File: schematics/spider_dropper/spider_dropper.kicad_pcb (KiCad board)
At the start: 2 copper layers, 80 x 20 mm, 10 parts, among them J1 12V DC, J2 JST_XH_3, J3 JST_XH_2, Q1 IRLZ34N, SW1 ZX40E20C01

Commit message: I think I'm ready to order Rev. D PCBs.
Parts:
- J2: renamed from J1; value 12V DC -> PJ-044AH
- renumbered J2 to J1
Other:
- board text added: "GND"
- board text added: "VIN"
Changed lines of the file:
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@@
 	(net 1 "+12V")
 	(net 2 "GND")
-	(net 3 "unconnected-(J1-Pad3)")
-	(net 4 "unconnected-(SW1-C-Pad2)")
-	(net 5 "/MOTOR+")
-	(net 6 "/MOTOR-")
-	(net 7 "/MOTION")
+	(net 3 "unconnected-(SW1-C-Pad2)")
+	(net 4 "/MOTOR+")
+	(net 5 "/MOTOR-")
+	(net 6 "/MOTION")
+	(net 7 "unconnected-(J2-Pad3)")
 	(footprint "Diode_THT:D_A-405_P7.62mm_Horizontal"
 		(layer "F.Cu")
@@
 			(remove_unused_layers no)
 			(roundrect_rratio 0.138889)
-			(net 5 "/MOTOR+")
+			(net 4 "/MOTOR+")
 			(pinfunction "K")
 			(pintype "passive")
@@
 			(layers "*.Cu" "*.Mask")
 			(remove_unused_layers no)
-			(net 6 "/MOTOR-")
+			(net 5 "/MOTOR-")
 			(pinfunction "A")
 			(pintype "passive")
@@
 			(layers "*.Cu" "*.Mask")
 			(remove_unused_layers no)
-			(net 7 "/MOTION")
+			(net 6 "/MOTION")
 			(pintype "passive")
 		)
@@
 		(at 116.5 104.8)
 		(descr "Barrel Jack, 2.0mm ID, 5.5mm OD, Vertical, THT, 5 Amp")
-		(property "Reference" "J1"
+		(property "Reference" "J2"
 			(at 4.2 8.1 0)
 			(unlocked yes)
@@
 			)
 		)
-		(property "Value" "12V DC"
+		(property "Value" "PJ-044AH"
 			(at 0 7.57 0)
 			(unlocked yes)
@@
 			(remove_unused_layers no)
 			(roundrect_rratio 0.15)
-			(net 3 "unconnected-(J1-Pad3)")
+			(net 7 "unconnected-(J2-Pad3)")
 			(pintype "passive+no_connect")
 			(thermal_bridge_angle 45)
@@
 			(remove_unused_layers no)
 			(roundrect_rratio 0.147059)
-			(net 5 "/MOTOR+")
+			(net 4 "/MOTOR+")
 			(pinfunction "Pin_1")
 			(pintype "passive")
@@
 			(layers "*.Cu" "*.Mask")
 			(remove_unused_layers no)
-			(net 6 "/MOTOR-")
+			(net 5 "/MOTOR-")
 			(pinfunction "Pin_2")
 			(pintype "passive")
@@
 			(layers "*.Cu" "*.Mask")
 			(remove_unused_layers no)
-			(net 7 "/MOTION")
+			(net 6 "/MOTION")
 			(pinfunction "G")
 			(pintype "input")
@@
 			(layers "*.Cu" "*.Mask")
 			(remove_unused_layers no)
-			(net 6 "/MOTOR-")
+			(net 5 "/MOTOR-")
 			(pinfunction "D")
 			(pintype "passive")
@@
 			(layers "*.Cu" "*.Mask")
 			(remove_unused_layers no)
-			(net 5 "/MOTOR+")
+			(net 4 "/MOTOR+")
 			(pintype "passive")
 		)
@@
 		(descr "JST XH series connector, B3B-XH-AM, with boss (http://www.jst-mfg.com/product/pdf/eng/eXH.pdf), generated with kicad-footprint-generator")
 		(tags "connector JST XH vertical boss")
-		(property "Reference" "J2"
+		(property "Reference" "J1"
 			(at 6.8 -3.375 0)
 			(layer "F.SilkS")
@@
 			(remove_unused_layers no)
 			(roundrect_rratio 0.147059)
-			(net 5 "/MOTOR+")
+			(net 4 "/MOTOR+")
 			(pinfunction "Pin_1")
 			(pintype "passive")
@@
 			(layers "*.Cu" "*.Mask")
 			(remove_unused_layers no)
-			(net 7 "/MOTION")
+			(net 6 "/MOTION")
 			(pinfunction "Pin_2")
 			(pintype "passive")
@@
 		(tags "mountinghole M3")
 		(property "Reference" "H1"
-			(at -4.3 -1.4 180)
+			(at 6.3 -1.4 180)
 			(layer "B.SilkS")
 			(effects
@@
 			(layers "*.Cu" "*.Mask")
 			(remove_unused_layers no)
-			(net 4 "unconnected-(SW1-C-Pad2)")
+			(net 3 "unconnected-(SW1-C-Pad2)")
 			(pinfunction "C")
 			(pintype "passive+no_connect")
@@
 			(layers "*.Cu" "*.Mask")
 			(remove_unused_layers no)
-			(net 6 "/MOTOR-")
+			(net 5 "/MOTOR-")
 			(pinfunction "A")
 			(pintype "passive")
@@
 	)
 	(gr_line
-		(start 172.9 113.3)
-		(end 171.4 110.7)
+		(start 175 113.3)
+		(end 175 117.1)
 		(stroke
 			(width 0.1)
-			(type default)
+			(type dot)
 		)
 		(layer "F.SilkS")
 	)
-	(gr_poly
-		(pts
-			(xy 171.4 110.7) (xy 168.4 110.7) (xy 166.8 113.3) (xy 168.4 115.9) (xy 171.4 115.9) (xy 172.9 113.3)
+	(gr_arc
+		(start 164.8 113.3)
+		(mid 169.9 108.2)
+		(end 175 113.3)
+		(stroke
+			(width 0.1)
+			(type dot)
 		)
+		(layer "F.SilkS")
+	)
+	(gr_line
+		(start 164.8 113.3)
+		(end 164.8 117.1)
 		(stroke
 			(width 0.1)
-			(type solid)
+			(type dot)
 		)
-		(fill no)
 		(layer "F.SilkS")
 	)
 	(gr_rect
-		(start 164.35 100.8)
-		(end 177.45 106.9)
+		(start 163.35 100.25)
+		(end 176.45 106.35)
 		(stroke
 			(width 0.1)
@@
 	)
 	(gr_rect
-		(start 164.35 100.8)
-		(end 177.45 106.9)
+		(start 163.35 100.25)
+		(end 176.45 106.35)
 		(stroke
 			(width 0.1)
@@
 		)
 	)
+	(gr_text "VIN"
+		(at 116.5 103.3 0)
+		(layer "F.SilkS")
+		(effects
+			(font
+				(size 1 1)
+				(thickness 0.15)
+			)
+			(justify bottom)
+		)
+	)
+	(gr_text "GND"
+		(at 116.5 109.6 0)
+		(layer "F.SilkS")
+		(effects
+			(font
+				(size 1 1)
+				(thickness 0.15)
+			)
+			(justify bottom)
+		)
+	)
 	(gr_text "Rev. D - 2025"
-		(at 171 108.5 0)
+		(at 169.9 107.9 0)
 		(layer "F.SilkS")
 		(effects
@@
 	)
 	(gr_text "Slightly Smarter\nSpider Dropper\nAdrian McCarthy"
-		(at 170.95 103.9 0)
+		(at 169.9 103.3 0)
 		(layer "F.SilkS")
 		(effects
@@
 	)
 	(gr_text "M3"
-		(at 166.7 113.3 0)
+		(at 177.3 113.3 0)
 		(layer "B.SilkS")
 		(effects
@@
 	)
 	(gr_text "Slightly Smarter\nSpider Dropper\nAdrian McCarthy"
-		(at 170.95 103.9 0)
+		(at 169.9 103.3 0)
 		(layer "B.SilkS")
 		(effects
@@
 	)
 	(gr_text "Rev. D - 2025"
-		(at 171 108.5 0)
+		(at 169.9 107.9 0)
 		(layer "B.SilkS")
 		(effects
@@
 		(width 0.2)
 		(layer "F.Cu")
-		(net 5)
+		(net 4)
 	)
 	(segment
@@
 		(width 0.2)
 		(layer "F.Cu")
-		(net 5)
+		(net 4)
 	)
 	(segment
@@
 		(width 0.2)
 		(layer "F.Cu")
-		(net 5)
+		(net 4)
 	)
 	(segment
@@
 		(width 0.2)
 		(layer "F.Cu")
-		(net 5)
+		(net 4)
 	)
 	(segment
@@
 		(width 0.2)
 		(layer "F.Cu")
-		(net 5)
+		(net 4)
 	)
 	(segment
@@
 		(width 0.2)
 		(layer "F.Cu")
-		(net 5)
+		(net 4)
 	)
 	(segment
@@
 		(width 0.2)
 		(layer "F.Cu")
-		(net 5)
+		(net 4)
 	)
 	(segment
@@
 		(width 0.2)
 		(layer "F.Cu")
-		(net 6)
+		(net 5)
 	)
 	(segment
@@
 		(width 0.2)
 		(layer "F.Cu")
-		(net 6)
+		(net 5)
 	)
 	(segment
@@
 		(width 0.2)
 		(layer "F.Cu")
-		(net 6)
+		(net 5)
 	)
 	(segment
@@
 		(width 0.2)
 		(layer "F.Cu")
-		(net 6)
+		(net 5)
 	)
 	(segment
@@
 		(width 0.2)
 		(layer "F.Cu")
-		(net 6)
+		(net 5)
 	)
 	(segment
@@
 		(width 0.2)
 		(layer "F.Cu")
-		(net 6)
+		(net 5)
 	)
 	(segment
@@
 		(width 0.2)
 		(layer "F.Cu")
-		(net 6)
+		(net 5)
 	)
 	(segment
@@
 		(width 0.2)
 		(layer "F.Cu")
-		(net 6)
+		(net 5)
 	)
 	(segment
@@
 		(width 0.2)
 		(layer "F.Cu")
-		(net 6)
+		(net 5)
 	)
 	(segment
@@
 		(width 0.2)
 		(layer "F.Cu")
-		(net 7)
+		(net 6)
 	)
 	(segment
@@
 		(width 0.2)
 		(layer "F.Cu")
-		(net 7)
+		(net 6)
 	)
 	(segment
@@
 		(width 0.2)
 		(layer "F.Cu")
-		(net 7)
+		(net 6)
 	)
 	(segment
@@
 		(width 0.2)
 		(layer "F.Cu")
-		(net 7)
+		(net 6)
 	)
 	(zone
@@
 		)
 	)
+	(group ""
+		(members "2a1c117f-9e90-49bd-96d1-d0fd1d1256d9" "8e58b6e7-301e-48f4-91da-1958e2963ec6"
+			"e5bebbb6-7bee-4a3c-8b40-823a10df51a7"
+		)
+	)

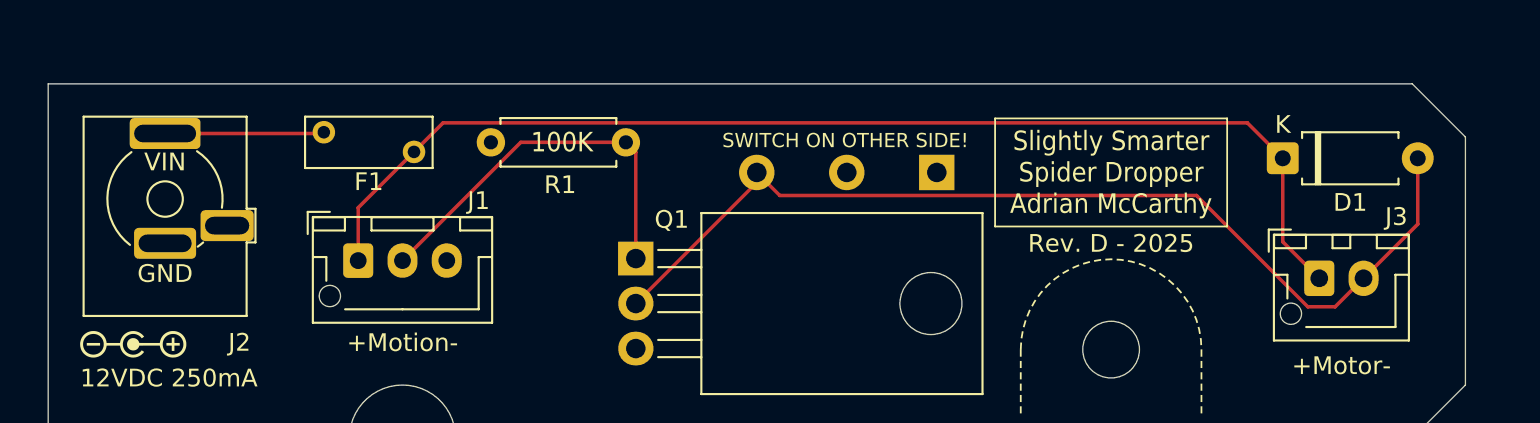
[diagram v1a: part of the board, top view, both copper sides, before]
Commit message: Updated PCB layout to Rev E.
Rev D was usable, but I discovered:

* The footprint for the vertical power jack was wrong.  I corrected it
in my footprint library and updated the PCB layout accordingly.

* The diode was a bit close to the cut corner.  I nudged it in to make
it easier to solder in place.
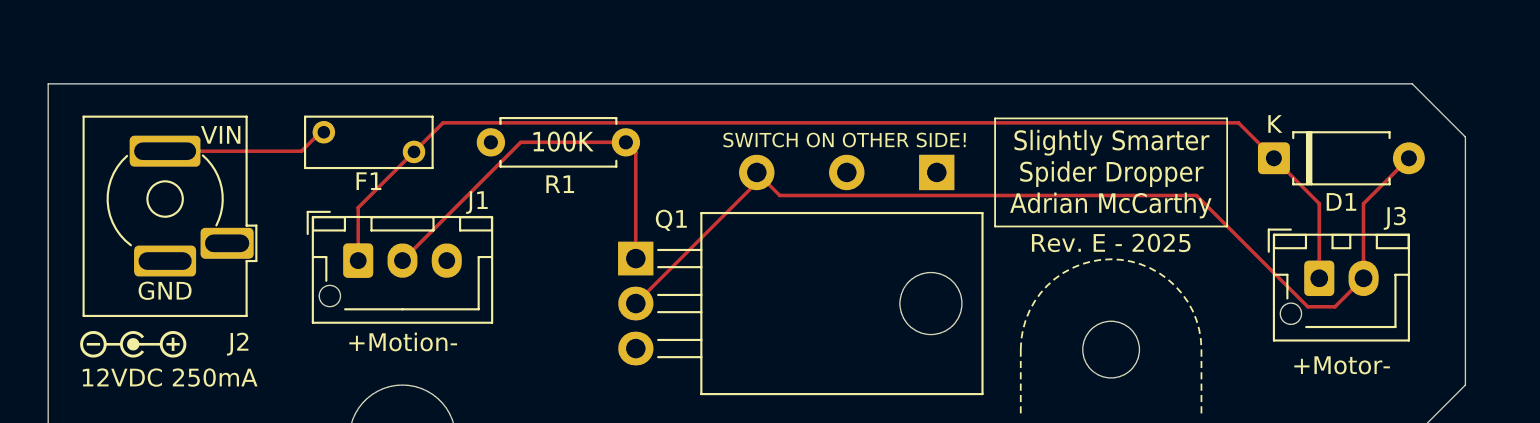
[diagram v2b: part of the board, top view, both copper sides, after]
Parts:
- moved D1 0.50 mm to (179.1, 102.5)
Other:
- board text added: "Rev. E - 2025"
- board text removed: "Rev. D - 2025"
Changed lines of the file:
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@@
 		(title "Slightly Smarter Simple Spider Dropper")
 		(date "2025-08-28")
-		(rev "D")
+		(rev "E")
 		(company "Adrian McCarthy")
 		(comment 1 "Improved clearance around J2 and J3")
@@
 		(comment 4 "Switched to MOSFET design")
 		(comment 5 "Changed index notch and added a mounting screw")
+		(comment 6 "corrected footprint for power connector")
+		(comment 7 "nudged diode away from corner")
 	)
 	(layers
@@
 	(footprint "Diode_THT:D_A-405_P7.62mm_Horizontal"
 		(layer "F.Cu")
-		(at 179.59 102.5)
+		(at 179.09 102.5)
 		(descr "Diode, A-405 series, Axial, Horizontal, pin pitch=7.62mm, length*diameter=5.2*2.7mm^2, http://www.diodes.com/_files/packages/A-405.pdf")
 		(tags "Diode A-405 series Axial Horizontal pin pitch 7.62mm  length 5.2mm diameter 2.7mm")
@@
 		(fp_line
 			(start 4.6 -4.65)
-			(end 4.6 0.55)
+			(end 4.6 1.5)
 			(stroke
 				(width 0.12)
@@
 		)
 		(fp_line
-			(start 4.6 0.55)
-			(end 5.1 0.55)
+			(start 4.6 1.5)
+			(end 5.15 1.5)
 			(stroke
 				(width 0.12)
@@
 		)
 		(fp_line
-			(start 4.6 2.45)
+			(start 4.6 3.5)
 			(end 4.6 6.6)
 			(stroke
@@
 		)
 		(fp_line
-			(start 5.1 0.55)
-			(end 5.1 2.45)
+			(start 5.15 1.5)
+			(end 5.15 3.5)
 			(stroke
 				(width 0.12)
@@
 		)
 		(fp_line
-			(start 5.1 2.45)
-			(end 4.6 2.45)
+			(start 5.15 3.5)
+			(end 4.6 3.5)
 			(stroke
 				(width 0.12)
@@
 		)
 		(fp_arc
-			(start -1.980744 2.590203)
-			(mid -3.260364 -0.050238)
-			(end -1.9 -2.65)
+			(start -1.93 2.61)
+			(mid -3.243103 0.138852)
+			(end -2.146021 -2.435487)
 			(stroke
 				(width 0.12)
@@
 		)
 		(fp_arc
-			(start 1.8 -2.7)
-			(mid 2.969454 -1.308564)
-			(end 3.207262 0.493425)
-			(stroke
-				(width 0.12)
-				(type default)
-			)
-			(layer "F.SilkS")
-		)
-		(fp_arc
-			(start 2.15 2.45)
-			(mid 1.999787 2.574073)
-			(end 1.842429 2.68895)
+			(start 2.13 -2.46)
+			(mid 3.195087 -0.616373)
+			(end 2.892228 1.491149)
 			(stroke
 				(width 0.12)
@@
 		(fp_line
 			(start 4.75 -4.75)
-			(end 4.75 0.4)
+			(end 4.75 1.4)
 			(stroke
 				(width 0.05)
@@
 		)
 		(fp_line
-			(start 4.75 0.4)
-			(end 5.25 0.4)
+			(start 4.75 1.4)
+			(end 5.25 1.4)
 			(stroke
 				(width 0.05)
@@
 		)
 		(fp_line
-			(start 4.75 2.6)
+			(start 4.75 3.6)
 			(end 4.75 6.7)
 			(stroke
@@
 		)
 		(fp_line
-			(start 5.25 0.4)
-			(end 5.25 2.6)
+			(start 5.25 1.4)
+			(end 5.25 3.6)
 			(stroke
 				(width 0.05)
@@
 		)
 		(fp_line
-			(start 5.25 2.6)
-			(end 4.75 2.6)
+			(start 5.25 3.6)
+			(end 4.75 3.6)
 			(stroke
 				(width 0.05)
@@
 		)
 		(pad "1" thru_hole roundrect
-			(at 0 -3.7)
+			(at 0 -2.7)
 			(size 4 1.75)
 			(drill oval 3.5 1)
@@
 		)
 		(pad "2" thru_hole roundrect
-			(at 0 2.5)
+			(at 0 3.5)
 			(size 3.5 1.75)
 			(drill oval 3 1)
@@
 		)
 		(pad "3" thru_hole roundrect
-			(at 3.5 1.5)
+			(at 3.5 2.5)
 			(size 3 1.75)
 			(drill oval 2.5 1)
@@
 	)
 	(gr_text "VIN"
-		(at 116.5 103.3 0)
+		(at 119.7 101.8 0)
 		(layer "F.SilkS")
 		(effects
@@
 	)
 	(gr_text "GND"
-		(at 116.5 109.6 0)
+		(at 116.5 110.6 0)
 		(layer "F.SilkS")
 		(effects
@@
 		)
 	)
-	(gr_text "Rev. D - 2025"
+	(gr_text "Rev. E - 2025"
 		(at 169.9 107.9 0)
 		(layer "F.SilkS")
@@
 		)
 	)
-	(gr_text "Rev. D - 2025"
+	(gr_text "Rev. E - 2025"
 		(at 169.9 107.9 0)
 		(layer "B.SilkS")
@@
 	)
 	(segment
-		(start 116.5 101.1)
-		(end 125.39 101.1)
+		(start 125.46 101.03)
+		(end 125.27 101.03)
 		(width 0.2)
 		(layer "F.Cu")
@@
 	)
 	(segment
-		(start 116.5 101)
-		(end 116.4 101.1)
+		(start 125.27 101.03)
+		(end 124.2 102.1)
 		(width 0.2)
 		(layer "F.Cu")
@@
 	)
 	(segment
-		(start 116.6 101)
-		(end 116.5 101.1)
+		(start 124.2 102.1)
+		(end 116.5 102.1)
 		(width 0.2)
 		(layer "F.Cu")
@@
 	)
 	(segment
-		(start 132.191 100.499)
-		(end 177.589 100.499)
+		(start 127.4 108.275)
+		(end 127.4 105.29)
 		(width 0.2)
 		(layer "F.Cu")
@@
 	)
 	(segment
-		(start 177.589 100.499)
-		(end 179.59 102.5)
+		(start 181.65 105.06)
+		(end 179.09 102.5)
 		(width 0.2)
 		(layer "F.Cu")
@@
 	)
 	(segment
-		(start 127.4 108.275)
-		(end 127.4 105.29)
+		(start 181.65 109.275)
+		(end 181.65 105.06)
 		(width 0.2)
 		(layer "F.Cu")
@@
 	)
 	(segment
-		(start 130.55 102.14)
+		(start 177.089 100.499)
 		(end 132.191 100.499)
 		(width 0.2)
@@
 	)
 	(segment
-		(start 127.4 105.29)
-		(end 130.55 102.14)
+		(start 179.09 102.5)
+		(end 177.089 100.499)
 		(width 0.2)
 		(layer "F.Cu")
@@
 	)
 	(segment
-		(start 179.59 107.215)
-		(end 181.65 109.275)
+		(start 127.4 105.29)
+		(end 130.55 102.14)
 		(width 0.2)
 		(layer "F.Cu")
@@
 	)
 	(segment
-		(start 179.59 102.5)
-		(end 179.59 107.215)
+		(start 132.191 100.499)
+		(end 130.55 102.14)
 		(width 0.2)
 		(layer "F.Cu")
@@
 	)
 	(segment
-		(start 187.21 106.215)
-		(end 184.15 109.275)
+		(start 186.71 102.5)
+		(end 184.15 105.06)
 		(width 0.2)
 		(layer "F.Cu")
@@
 	)
 	(segment
-		(start 187.21 102.5)
-		(end 187.21 106.215)
+		(start 184.15 105.06)
+		(end 184.15 109.275)
 		(width 0.2)
 		(layer "F.Cu")
